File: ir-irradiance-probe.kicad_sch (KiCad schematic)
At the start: 50 parts, among them J1 USB-C_UJC-HP-3-SMT-TR, J2 SM04B-SRSS-TB-LF-SN, J3 PinHeader_1x2_P2.54mm_Drill1.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, J4 Conn_BNC_031-70526-21, SW1 MSS3-V-T_R, U1 TLV70033_SC70, U2 AD8604ARUZ, U3 ADC101C027CIMK

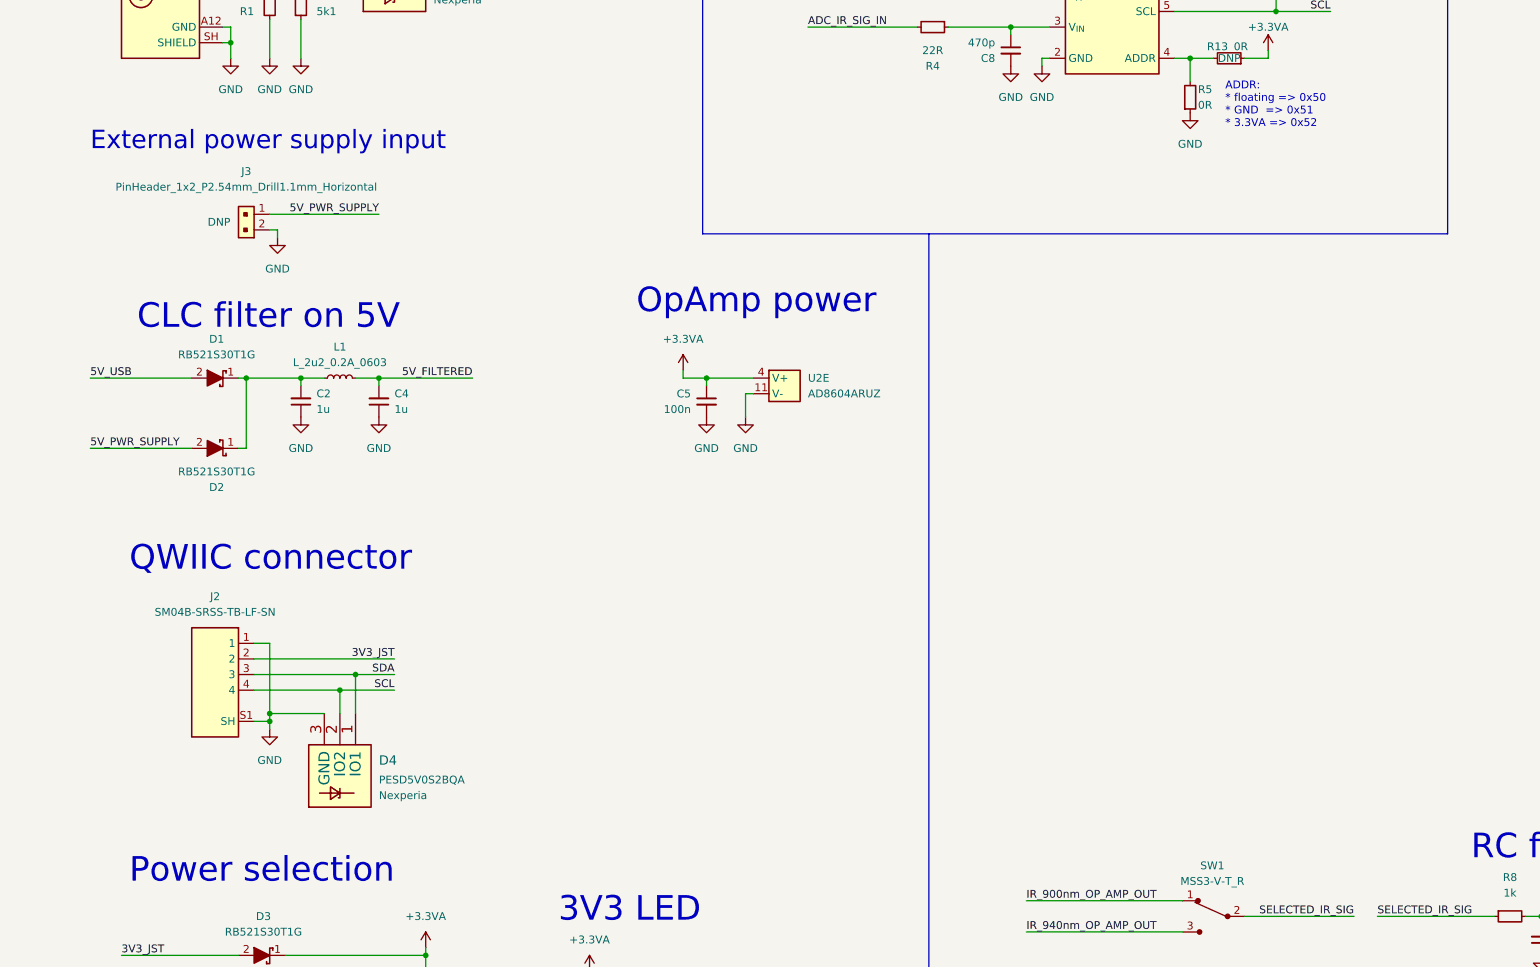
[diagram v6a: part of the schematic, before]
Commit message: [#47284] Unified text size on schematic
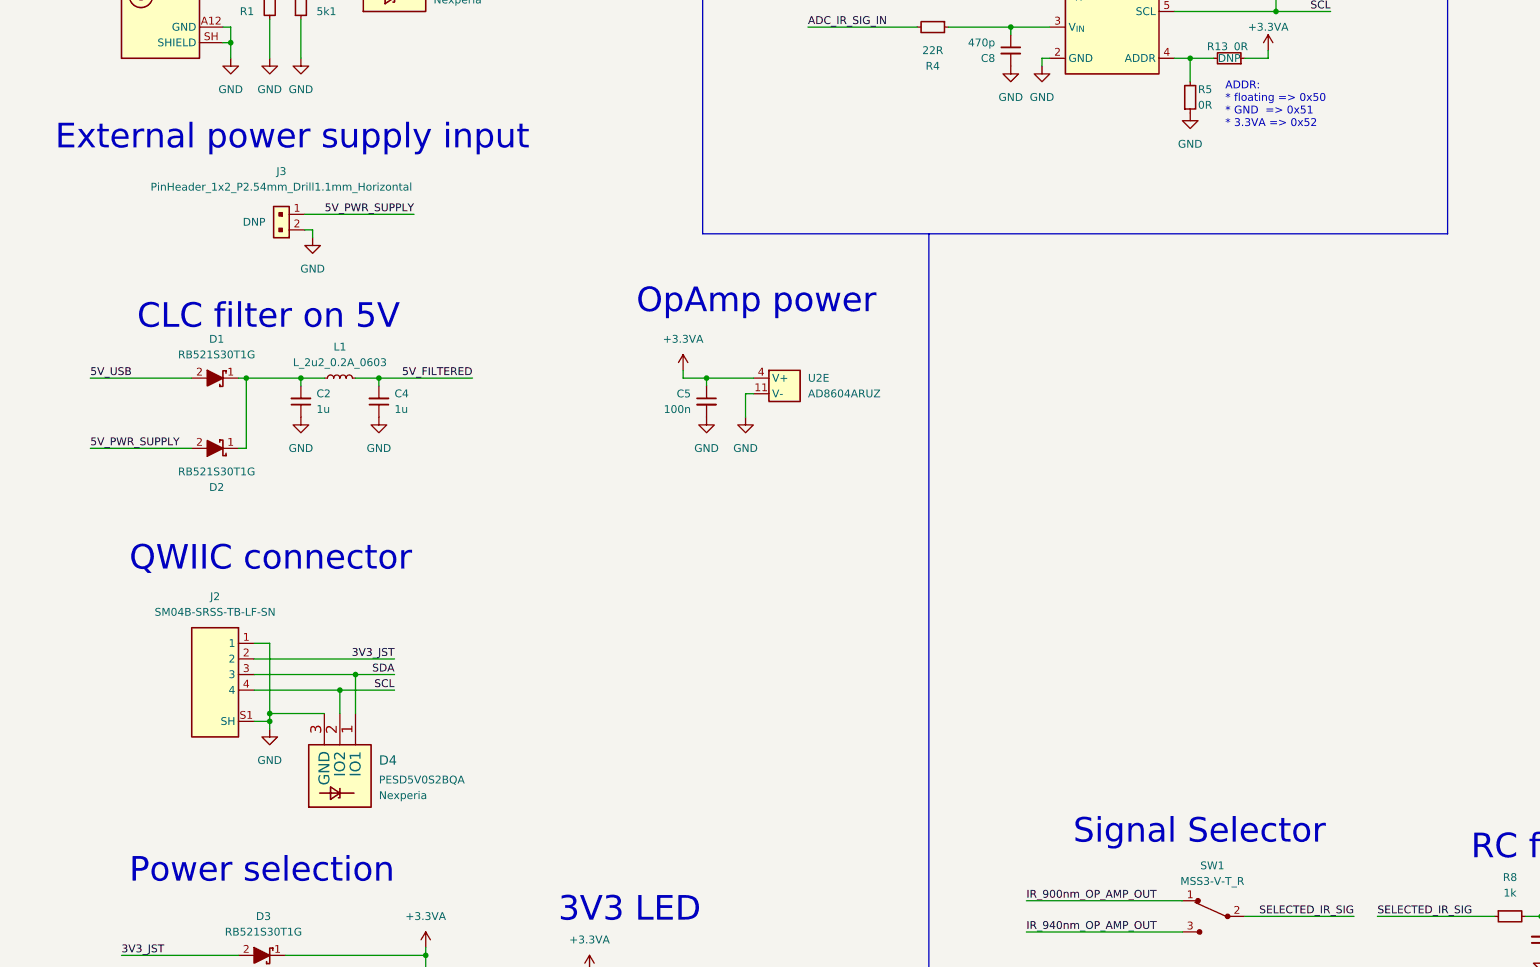
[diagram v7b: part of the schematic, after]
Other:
- note added: "Signal Selector"
- moved on the sheet: J3
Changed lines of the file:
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@@
     (stroke (width 0) (type default) (color 0 0 0 0))
   )
-  (wire (pts (xy 54.61 99.06) (xy 53.34 99.06))
+  (wire (pts (xy 60.325 99.06) (xy 59.055 99.06))
     (stroke (width 0) (type default) (color 0 0 0 0))
   )
@@
     (stroke (width 0) (type default) (color 0 0 0 0))
   )
-  (wire (pts (xy 53.34 96.52) (xy 71.12 96.52))
+  (wire (pts (xy 59.055 96.52) (xy 76.835 96.52))
     (stroke (width 0) (type default) (color 0 0 0 0))
   )
@@
     (stroke (width 0) (type default) (color 0 0 0 0))
   )
-  (wire (pts (xy 54.61 100.33) (xy 54.61 99.06))
+  (wire (pts (xy 60.325 100.33) (xy 60.325 99.06))
     (stroke (width 0) (type default) (color 0 0 0 0))
   )
@@
   (wire (pts (xy 339.09 124.46) (xy 339.09 128.27))
     (stroke (width 0) (type default) (color 0 0 0 0))
+  )
+  (text "Signal Selector" (at 184.15 199.39 0)
+    (effects (font (size 4 4)) (justify left bottom))
   )
   (text "Digital Section" (at 152.4 22.86 0)
@@
     (effects (font (size 4 4)) (justify left bottom))
   )
-  (text "External power supply input" (at 24.13 86.36 0)
-    (effects (font (size 3 3)) (justify left bottom))
+  (text "External power supply input" (at 18.415 86.36 0)
+    (effects (font (size 4 4)) (justify left bottom))
   )
   (text "OpAmp power" (at 113.03 113.03 0)
@@
     (effects (font (size 1.27 1.27)) (justify right bottom))
   )
-  (label "5V_PWR_SUPPLY" (at 71.12 96.52 180)
+  (label "5V_PWR_SUPPLY" (at 76.835 96.52 180)
     (effects (font (size 1.27 1.27)) (justify right bottom))
   )
@@
     (pin "1")
   )
-  (symbol (lib_id "ir-irradiance-probe:GND") (at 54.61 100.33 0) (unit 1)
-    (in_bom yes) (on_board yes) (fields_autoplaced)
-    (property "Reference" "#PWR05" (id 0) (at 63.5 102.87 0)
-      (effects (font (size 1.27 1.27) (thickness 0.15)) (justify left bottom) hide)
-    )
-    (property "Value" "GND" (id 1) (at 54.61 105.41 0)
-      (effects (font (size 1.27 1.27) (thickness 0.15)))
-    )
-    (property "Footprint" "" (id 2) (at 63.5 107.95 0)
-      (effects (font (size 1.27 1.27) (thickness 0.15)) (justify left bottom) hide)
-    )
-    (property "Datasheet" "" (id 3) (at 63.5 113.03 0)
-      (effects (font (size 1.27 1.27) (thickness 0.15)) (justify left bottom) hide)
-    )
-    (property "Author" "Antmicro" (id 4) (at 63.5 107.95 0)
-      (effects (font (size 1.27 1.27) (thickness 0.15)) (justify left bottom) hide)
-    )
-    (property "License" "Apache-2.0" (id 5) (at 63.5 110.49 0)
+  (symbol (lib_id "ir-irradiance-probe:GND") (at 60.325 100.33 0) (unit 1)
+    (in_bom yes) (on_board yes) (fields_autoplaced)
+    (property "Reference" "#PWR05" (id 0) (at 69.215 102.87 0)
+      (effects (font (size 1.27 1.27) (thickness 0.15)) (justify left bottom) hide)
+    )
+    (property "Value" "GND" (id 1) (at 60.325 105.41 0)
+      (effects (font (size 1.27 1.27) (thickness 0.15)))
+    )
+    (property "Footprint" "" (id 2) (at 69.215 107.95 0)
+      (effects (font (size 1.27 1.27) (thickness 0.15)) (justify left bottom) hide)
+    )
+    (property "Datasheet" "" (id 3) (at 69.215 113.03 0)
+      (effects (font (size 1.27 1.27) (thickness 0.15)) (justify left bottom) hide)
+    )
+    (property "Author" "Antmicro" (id 4) (at 69.215 107.95 0)
+      (effects (font (size 1.27 1.27) (thickness 0.15)) (justify left bottom) hide)
+    )
+    (property "License" "Apache-2.0" (id 5) (at 69.215 110.49 0)
       (effects (font (size 1.27 1.27) (thickness 0.15)) (justify left bottom) hide)
     )
@@
     (pin "2")
   )
-  (symbol (lib_id "ir-irradiance-probe:PinHeader_1x2_P2.54mm_Drill1.1mm_Horizontal") (at 53.34 96.52 0) (mirror y) (unit 1)
+  (symbol (lib_id "ir-irradiance-probe:PinHeader_1x2_P2.54mm_Drill1.1mm_Horizontal") (at 59.055 96.52 0) (mirror y) (unit 1)
     (in_bom yes) (on_board yes)
-    (property "Reference" "J3" (id 0) (at 49.53 89.535 0)
-      (effects (font (size 1.27 1.27) (thickness 0.15)))
-    )
-    (property "Value" "PinHeader_1x2_P2.54mm_Drill1.1mm_Horizontal" (id 1) (at 49.53 92.075 0)
-      (effects (font (size 1.27 1.27) (thickness 0.15)))
-    )
-    (property "Footprint" "ir-irradiance-probe-footprints:PinHeader_1x02_P2.54mm_Horizontal" (id 2) (at 33.02 106.68 0)
-      (effects (font (size 1.27 1.27) (thickness 0.15)) (justify left bottom) hide)
-    )
-    (property "Datasheet" "https://www.we-online.com/components/products/datasheet/61300211021.pdf" (id 3) (at 33.02 109.22 0)
-      (effects (font (size 1.27 1.27) (thickness 0.15)) (justify left bottom) hide)
-    )
-    (property "MPN" "61300211021" (id 4) (at 33.02 111.76 0)
-      (effects (font (size 1.27 1.27) (thickness 0.15)) (justify left bottom) hide)
-    )
-    (property "Manufacturer" "Würth Elektronik" (id 5) (at 33.02 114.3 0)
-      (effects (font (size 1.27 1.27) (thickness 0.15)) (justify left bottom) hide)
-    )
-    (property "Author" "Antmicro" (id 6) (at 33.02 116.84 0)
-      (effects (font (size 1.27 1.27) (thickness 0.15)) (justify left bottom) hide)
-    )
-    (property "License" "Apache-2.0" (id 7) (at 33.02 119.38 0)
-      (effects (font (size 1.27 1.27) (thickness 0.15)) (justify left bottom) hide)
-    )
-    (property "DNP" "DNP" (id 8) (at 45.085 97.79 0))
-    (pin "1")
-    (pin "2")
+    (property "Reference" "J3" (id 0) (at 55.245 89.535 0)
+      (effects (font (size 1.27 1.27) (thickness 0.15)))
+    )
+    (property "Value" "PinHeader_1x2_P2.54mm_Drill1.1mm_Horizontal" (id 1) (at 55.245 92.075 0)
+      (effects (font (size 1.27 1.27) (thickness 0.15)))
+    )
+    (property "Footprint" "ir-irradiance-probe-footprints:PinHeader_1x02_P2.54mm_Horizontal" (id 2) (at 38.735 106.68 0)
+      (effects (font (size 1.27 1.27) (thickness 0.15)) (justify left bottom) hide)
+    )
+    (property "Datasheet" "https://www.we-online.com/components/products/datasheet/61300211021.pdf" (id 3) (at 38.735 109.22 0)
+      (effects (font (size 1.27 1.27) (thickness 0.15)) (justify left bottom) hide)
+    )
+    (property "MPN" "61300211021" (id 4) (at 38.735 111.76 0)
+      (effects (font (size 1.27 1.27) (thickness 0.15)) (justify left bottom) hide)
+    )
+    (property "Manufacturer" "Würth Elektronik" (id 5) (at 38.735 114.3 0)
+      (effects (font (size 1.27 1.27) (thickness 0.15)) (justify left bottom) hide)
+    )
+    (property "Author" "Antmicro" (id 6) (at 38.735 116.84 0)
+      (effects (font (size 1.27 1.27) (thickness 0.15)) (justify left bottom) hide)
+    )
+    (property "License" "Apache-2.0" (id 7) (at 38.735 119.38 0)
+      (effects (font (size 1.27 1.27) (thickness 0.15)) (justify left bottom) hide)
+    )
+    (property "DNP" "DNP" (id 8) (at 50.8 97.79 0))
+    (pin "1")
+    (pin "2")

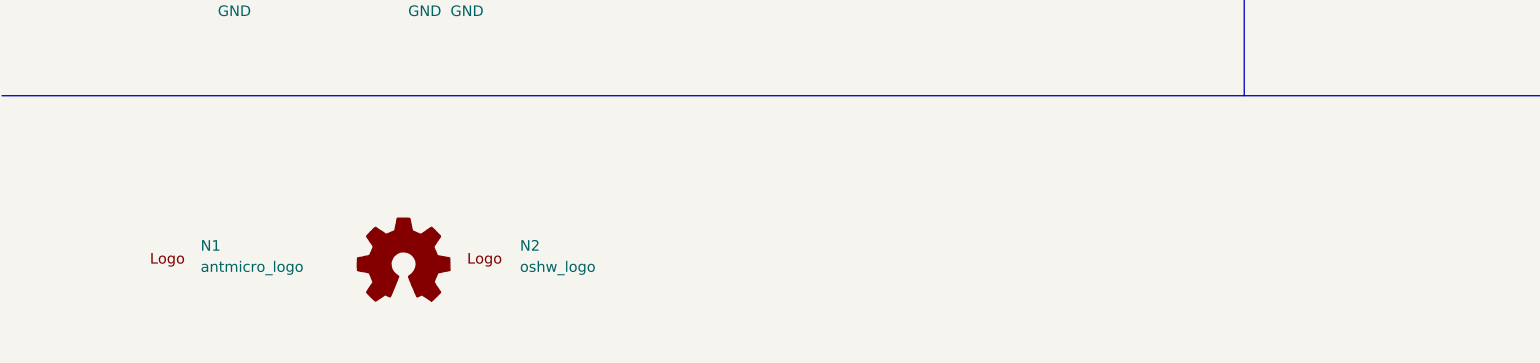
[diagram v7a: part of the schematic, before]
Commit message: [#47284] Update project info and add logo
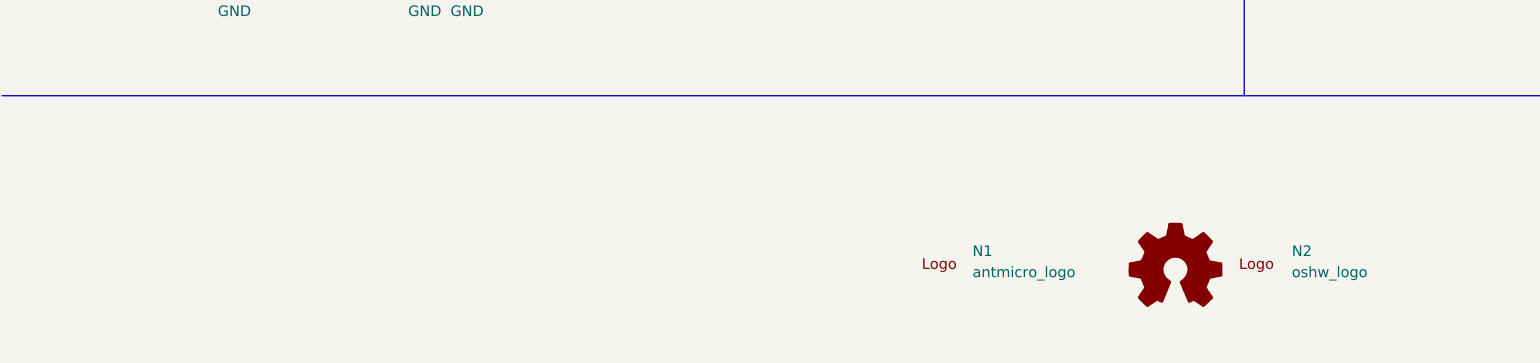
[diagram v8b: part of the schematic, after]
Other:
- company: (none) -> Antmicro Ltd
- title: (none) -> IR irradiance probe
- moved on the sheet: N1, N2
